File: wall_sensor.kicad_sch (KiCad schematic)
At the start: 9 parts, among them J1 Conn_01x04_Pin, Q1 LTR-4206, U1 BCR421UW6-7

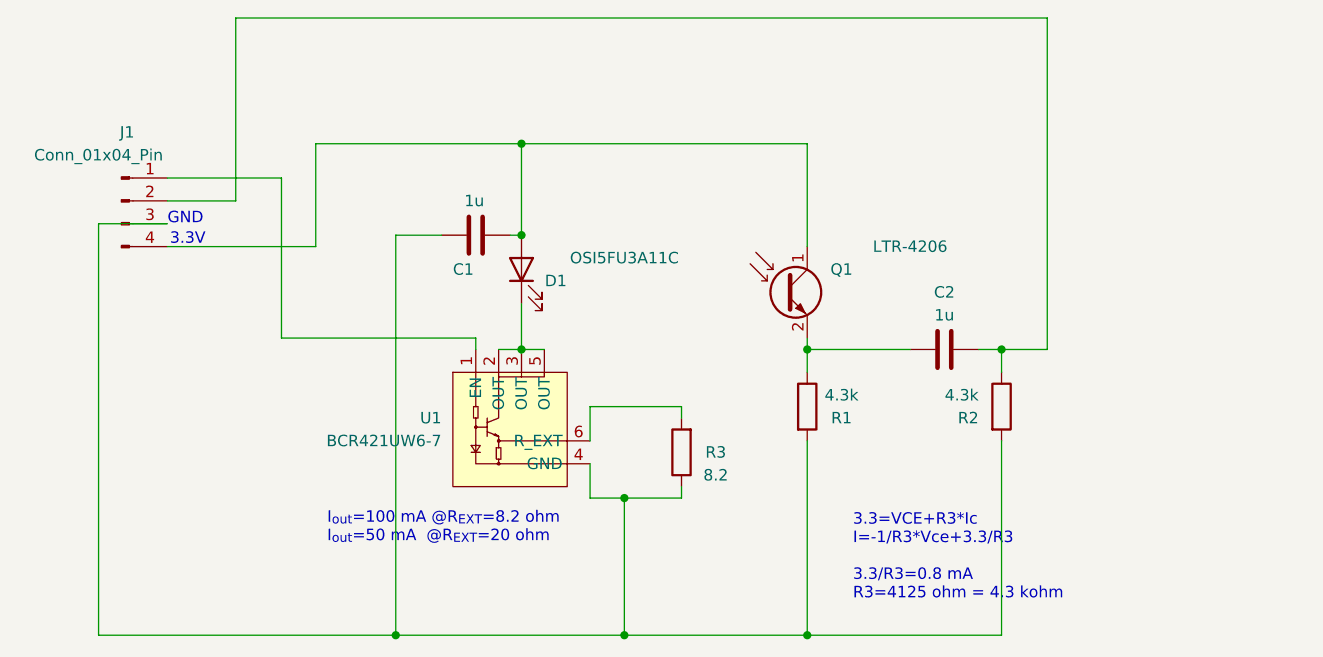
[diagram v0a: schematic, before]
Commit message: 壁センサ修正
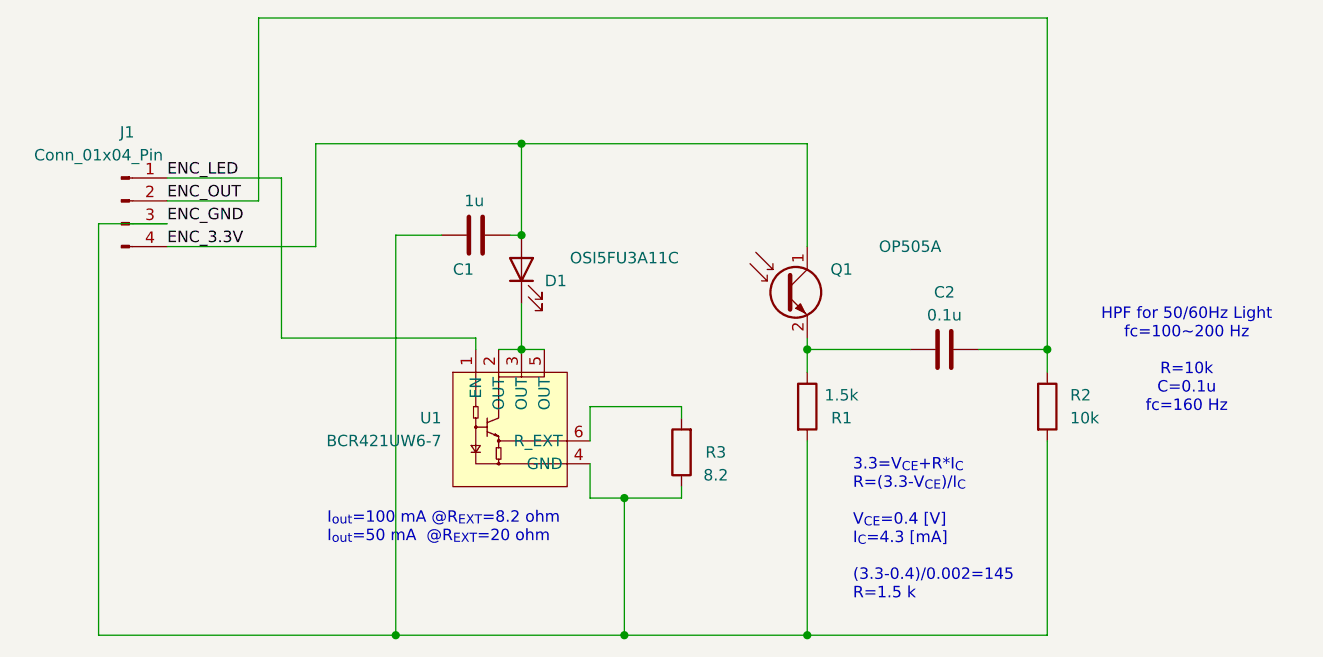
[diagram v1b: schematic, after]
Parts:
- C2: value 1u -> 0.1u
- Q1: value LTR-4206 -> OP505A; footprint makyi_mouse:LED -> makyi_mouse:LED_photo_tr; order_URL https://www.digikey.jp/ja/products/detail/liteon/LTR-4206/2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 -> https://www.digikey.jp/ja/products/detail/tt-electronics-op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
- R1: value 4.3k -> 1.5k
- R2: value 4.3k -> 10k
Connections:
- net ENC_LED: now reaches J1.1 (Pin_1), U1.1 (EN)
- net ENC_OUT: now reaches C2.1, J1.2 (Pin_2), R2.1
- net ENC_GND: now reaches C1.2, J1.3 (Pin_3), R1.2, R2.2, R3.1, U1.4 (GND)
- net ENC_3.3V: now reaches C1.1, D1.2 (A), J1.4 (Pin_4), Q1.1 (C)
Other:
- note added: "3.3=V_{CE}+R*I_{C} R=(3.3-V_{CE})/I_{C} V_{CE}=0.4 [V] I_{C}=4.3 [mA] (3.3-0.4)/0.002=145 R=1.5 k"
- note added: "HPF for 50/60Hz Light fc=100~200 Hz R=10k C=0.1u fc=160 Hz"
- note removed: "3.3=VCE+R3*Ic I=-1/R3*Vce+3.3/R3 3.3/R3=0.8 mA R3=4125 ohm = 4.3 kohm"
- note removed: "3.3V"
- note removed: "GND"
- moved on the sheet: R2
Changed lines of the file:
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@@
-	)
-	(junction
-		(at 175.26 99.06)
-		(diameter 0)
-		(color 0 0 0 0)
 	)
 	(junction
@@
 	)
 	(junction
+		(at 180.34 99.06)
+		(diameter 0)
+		(color 0 0 0 0)
+	)
+	(junction
 		(at 121.92 86.36)
 		(diameter 0)
@@
 	(wire
 		(pts
-			(xy 90.17 62.23) (xy 180.34 62.23)
+			(xy 92.71 62.23) (xy 180.34 62.23)
 		)
 		(stroke
@@
 	(wire
 		(pts
-			(xy 175.26 101.6) (xy 175.26 99.06)
+			(xy 180.34 101.6) (xy 180.34 99.06)
 		)
 		(stroke
@@
 	(wire
 		(pts
-			(xy 99.06 87.63) (xy 82.55 87.63)
-		)
-		(stroke
-			(width 0)
-			(type default)
-		)
-	)
-	(wire
-		(pts
 			(xy 121.92 99.06) (xy 124.46 99.06)
 		)
@@
 	(wire
 		(pts
-			(xy 90.17 82.55) (xy 82.55 82.55)
+			(xy 92.71 82.55) (xy 82.55 82.55)
 		)
 		(stroke
@@
 	(wire
 		(pts
-			(xy 153.67 130.81) (xy 175.26 130.81)
+			(xy 153.67 130.81) (xy 180.34 130.81)
+		)
+		(stroke
+			(width 0)
+			(type default)
+		)
+	)
+	(wire
+		(pts
+			(xy 82.55 87.63) (xy 99.06 87.63)
 		)
 		(stroke
@@
 	(wire
 		(pts
-			(xy 180.34 99.06) (xy 175.26 99.06)
-		)
-		(stroke
-			(width 0)
-			(type default)
-		)
-	)
-	(wire
-		(pts
 			(xy 120.65 86.36) (xy 121.92 86.36)
 		)
@@
 	(wire
 		(pts
-			(xy 175.26 109.22) (xy 175.26 130.81)
-		)
-		(stroke
-			(width 0)
-			(type default)
-		)
-	)
-	(wire
-		(pts
-			(xy 90.17 62.23) (xy 90.17 82.55)
+			(xy 180.34 109.22) (xy 180.34 130.81)
+		)
+		(stroke
+			(width 0)
+			(type default)
+		)
+	)
+	(wire
+		(pts
+			(xy 92.71 62.23) (xy 92.71 82.55)
 		)
 		(stroke
@@
 	(wire
 		(pts
-			(xy 172.72 99.06) (xy 175.26 99.06)
-		)
-		(stroke
-			(width 0)
-			(type default)
-		)
-	)
-	(text "GND"
+			(xy 172.72 99.06) (xy 180.34 99.06)
+		)
+		(stroke
+			(width 0)
+			(type default)
+		)
+	)
+	(text "HPF for 50/60Hz Light\nfc=100~200 Hz\n\nR=10k\nC=0.1u\nfc=160 Hz"
 		(exclude_from_sim no)
-		(at 84.582 84.582 0)
+		(at 195.834 100.33 0)
 		(effects
 			(font
@@
 		)
 	)
-	(text "3.3=VCE+R3*Ic\nI=-1/R3*Vce+3.3/R3\n\n3.3/R3=0.8 mA\nR3=4125 ohm = 4.3 kohm\n"
+	(text "3.3=V_{CE}+R*I_{C}\nR=(3.3-V_{CE})/I_{C}\n\nV_{CE}=0.4 [V]\nI_{C}=4.3 [mA]\n\n(3.3-0.4)/0.002=145\nR=1.5 k"
 		(exclude_from_sim no)
 		(at 158.75 127 0)
@@
 		)
 	)
-	(text "3.3V"
-		(exclude_from_sim no)
-		(at 84.836 86.868 0)
+	(label "ENC_GND"
+		(at 82.55 85.09 0)
+		(fields_autoplaced yes)
 		(effects
 			(font
 				(size 1.27 1.27)
 			)
+			(justify left bottom)
+		)
+	)
+	(label "ENC_LED"
+		(at 82.55 80.01 0)
+		(fields_autoplaced yes)
+		(effects
+			(font
+				(size 1.27 1.27)
+			)
+			(justify left bottom)
+		)
+	)
+	(label "ENC_OUT"
+		(at 82.55 82.55 0)
+		(fields_autoplaced yes)
+		(effects
+			(font
+				(size 1.27 1.27)
+			)
+			(justify left bottom)
+		)
+	)
+	(label "ENC_3.3V"
+		(at 82.55 87.63 0)
+		(fields_autoplaced yes)
+		(effects
+			(font
+				(size 1.27 1.27)
+			)
+			(justify left bottom)
 		)
 	)
@@
 			)
 		)
-		(property "Value" "1u"
+		(property "Value" "0.1u"
 			(at 168.91 95.25 90)
 			(effects
@@
 			)
 		)
-		(property "Value" "LTR-4206"
+		(property "Value" "OP505A"
 			(at 165.1 87.63 0)
 			(effects
@@
 			)
 		)
-		(property "Footprint" "makyi_mouse:LED"
+		(property "Footprint" "makyi_mouse:LED_photo_tr"
 			(at 156.21 90.17 0)
 			(effects
@@
 			)
 		)
-		(property "Datasheet" "https://optoelectronics.liteon.com/upload/download/DS-50-92-0072/R4206.pdf"
+		(property "Datasheet" "https://www.ttelectronics.com/TTElectronics/media/ProductFiles/Datasheet/OP505-506-535-705.pdf"
 			(at 151.13 92.71 0)
 			(effects
@@
 			)
 		)
-		(property "order_URL" "https://www.digikey.jp/ja/products/detail/liteon/LTR-4206/214965"
+		(property "order_URL" "https://www.digikey.jp/ja/products/detail/tt-electronics-optek-technology/OP505A/498692"
 			(at 151.13 92.71 0)
 			(effects
@@
 	(symbol
 		(lib_id "Device:R")
-		(at 175.26 105.41 0)
+		(at 180.34 105.41 0)
 		(unit 1)
 		(exclude_from_sim no)
@@
 		(fields_autoplaced yes)
 		(property "Reference" "R2"
-			(at 172.72 106.68 0)
-			(effects
-				(font
-					(size 1.27 1.27)
-				)
-				(justify right)
-			)
-		)
-		(property "Value" "4.3k"
-			(at 172.72 104.14 0)
-			(effects
-				(font
-					(size 1.27 1.27)
-				)
-				(justify right)
+			(at 182.88 104.1399 0)
+			(effects
+				(font
+					(size 1.27 1.27)
+				)
+				(justify left)
+			)
+		)
+		(property "Value" "10k"
+			(at 182.88 106.6799 0)
+			(effects
+				(font
+					(size 1.27 1.27)
+				)
+				(justify left)
 			)
 		)
 		(property "Footprint" "Resistor_SMD:R_0402_1005Metric"
-			(at 173.482 105.41 90)
+			(at 178.562 105.41 90)
 			(effects
 				(font
@@
 		)
 		(property "Datasheet" "~"
-			(at 175.26 105.41 0)
+			(at 180.34 105.41 0)
 			(effects
 				(font
@@
 		)
 		(property "Description" ""
-			(at 175.26 105.41 0)
+			(at 180.34 105.41 0)
 			(effects
 				(font
@@
 		)
 		(property "order_URL" "https://www.digikey.jp/ja/products/detail/yageo/RC0402FR-074K3L/726604"
-			(at 175.26 105.41 0)
+			(at 180.34 105.41 0)
 			(effects
 				(font
@@
 		)
 		(property "check_order" "-"
-			(at 175.26 105.41 0)
+			(at 180.34 105.41 0)
 			(effects
 				(font
@@
 			)
 		)
-		(property "Value" "4.3k"
+		(property "Value" "1.5k"
 			(at 157.48 104.14 0)
 			(effects
